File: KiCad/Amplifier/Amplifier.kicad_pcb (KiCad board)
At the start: 2 copper layers, 48 x 53 mm, 30 parts, among them J1 Screw_Terminal_01x03, J2 Screw_Terminal_01x03, Q1 NPN, Q2 NPN, U1 TL074

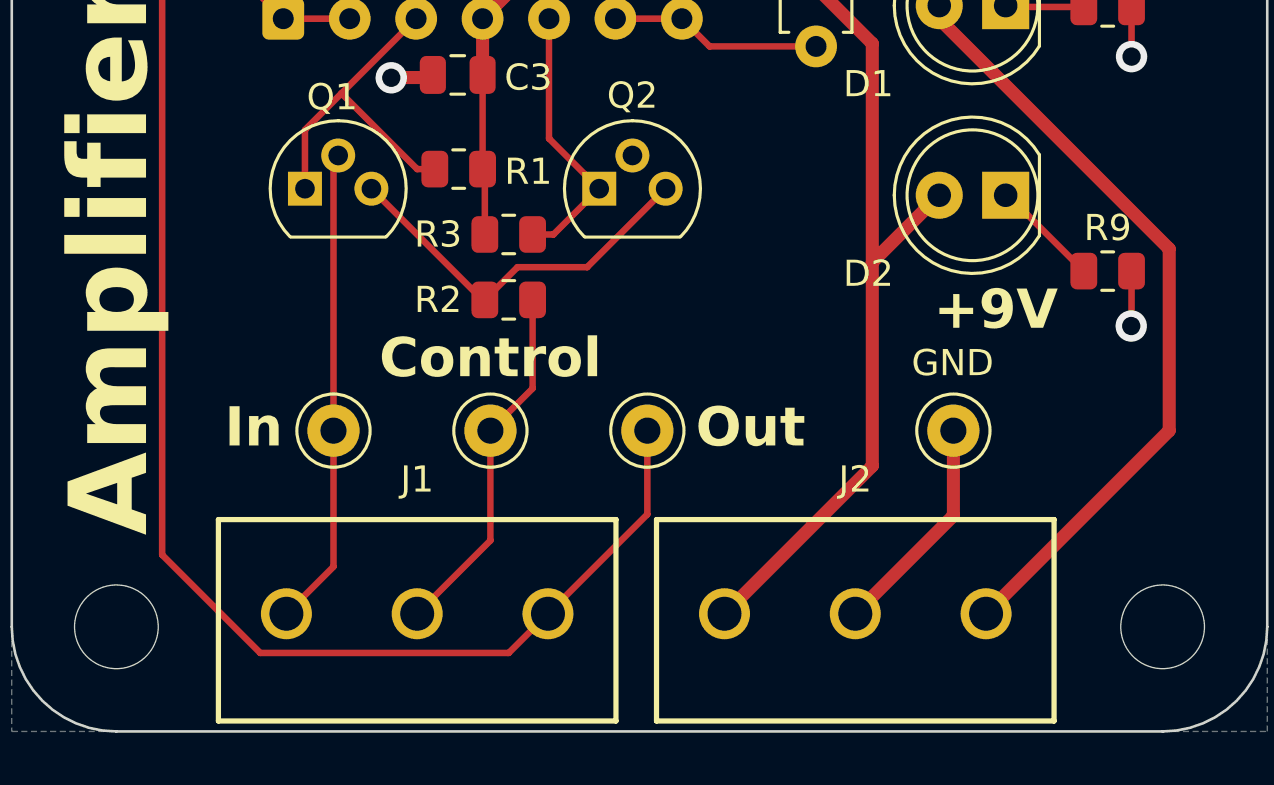
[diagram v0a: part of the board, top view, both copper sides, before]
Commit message: preparation to merge project back into one board
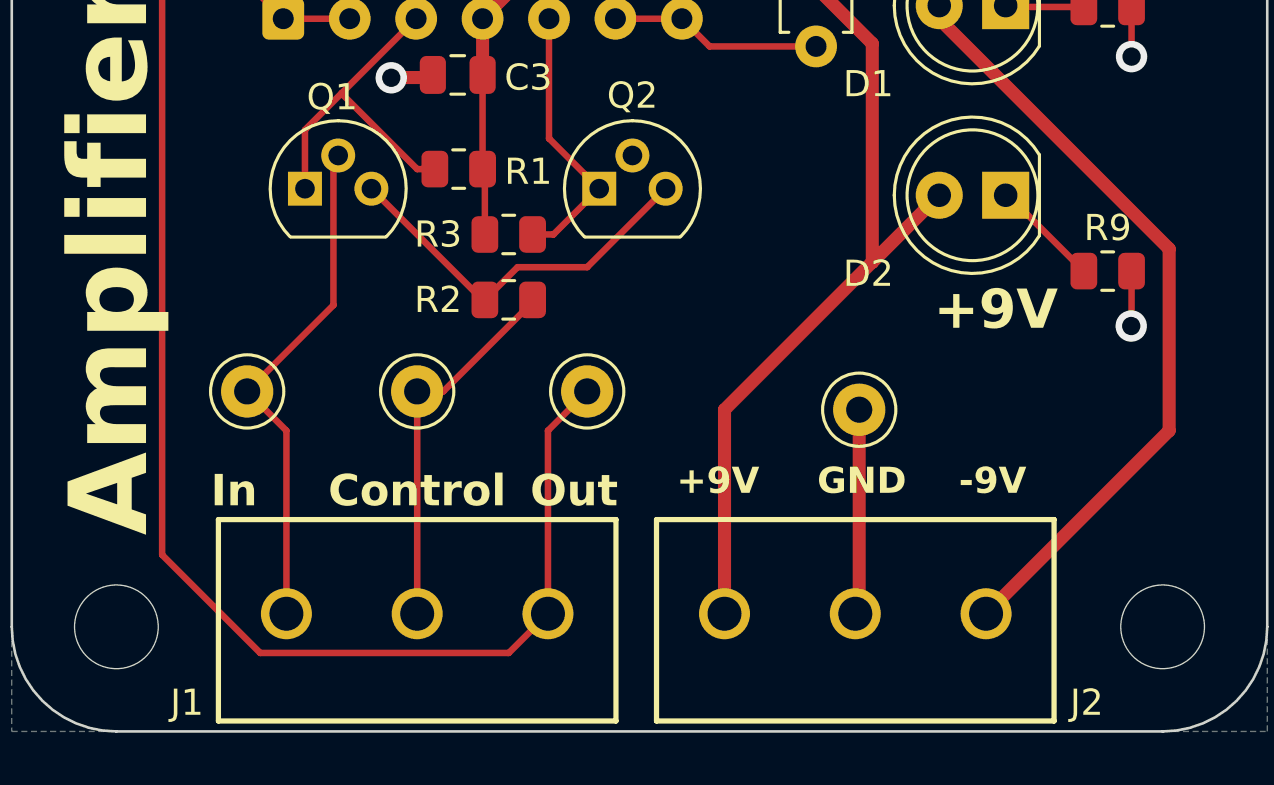
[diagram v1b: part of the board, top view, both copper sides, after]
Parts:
- moved TP4 3.69 mm to (74.4, 75.7)
- moved TP1 3.62 mm to (51.0, 75.0)
- moved TP2 3.18 mm to (57.5, 75.0)
- moved TP3 2.75 mm to (64.0, 75.0)
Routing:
- net /In: track 18.3 -> 19.6 mm
- net GND: track 17.8 -> 17.1 mm
- net /Control: track 13.8 -> 14.4 mm
- net /Out: track 75.2 -> 75.7 mm
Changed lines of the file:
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@@
 			(plot_on_all_layers_selection 0x00000000_00000000_00000000_00000000)
 			(disableapertmacros no)
-			(usegerberextensions no)
+			(usegerberextensions yes)
 			(usegerberattributes yes)
 			(usegerberadvancedattributes yes)
-			(creategerberjobfile yes)
+			(creategerberjobfile no)
 			(dashed_line_dash_ratio 12)
 			(dashed_line_gap_ratio 3)
@@
 			(outputformat 1)
 			(mirror no)
-			(drillshape 1)
+			(drillshape 0)
 			(scaleselection 1)
-			(outputdirectory "")
+			(outputdirectory "../../Build/Aug 20 2026/")
 		)
 	)
@@
 	(footprint "TestPoint:TestPoint_Keystone_5000-5004_Miniature"
 		(layer "F.Cu")
-		(at 78 76.5)
+		(at 74.4 75.7)
 		(descr "Keystone THM Miniature Test Point 5000-5004, http://www.keyelco.com/product-pdf.cfm?p=1309")
 		(tags "Through Hole Mount Test Points")
@@
 	(footprint "TestPoint:TestPoint_Keystone_5000-5004_Miniature"
 		(layer "F.Cu")
-		(at 66.3 76.5)
+		(at 64 75)
 		(descr "Keystone THM Miniature Test Point 5000-5004, http://www.keyelco.com/product-pdf.cfm?p=1309")
 		(tags "Through Hole Mount Test Points")
@@
 	(footprint "TestPoint:TestPoint_Keystone_5000-5004_Miniature"
 		(layer "F.Cu")
-		(at 54.3 76.5)
+		(at 51 75)
 		(descr "Keystone THM Miniature Test Point 5000-5004, http://www.keyelco.com/product-pdf.cfm?p=1309")
 		(tags "Through Hole Mount Test Points")
@@
 		(at 57.5 83.5)
 		(property "Reference" "J1"
-			(at 0 -5.135 0)
+			(at -8.8 3.4 0)
 			(layer "F.SilkS")
 			(effects
@@
 		(at 74.25 83.5)
 		(property "Reference" "J2"
-			(at 0 -5.135 0)
+			(at 8.85 3.4 0)
 			(layer "F.SilkS")
 			(effects
@@
 	(footprint "TestPoint:TestPoint_Keystone_5000-5004_Miniature"
 		(layer "F.Cu")
-		(at 60.3 76.5)
+		(at 57.5 75)
 		(descr "Keystone THM Miniature Test Point 5000-5004, http://www.keyelco.com/product-pdf.cfm?p=1309")
 		(tags "Through Hole Mount Test Points")
@@
 		(layer "Edge.Cuts")
 	)
+	(gr_text "+9V"
+		(at 69 79 0)
+		(layer "F.SilkS")
+		(effects
+			(font
+				(size 1 1)
+				(thickness 0.2)
+				(bold yes)
+			)
+			(justify bottom)
+		)
+	)
 	(gr_text "GND"
-		(at 76.4 74.5 0)
+		(at 74.5 79 0)
 		(layer "F.SilkS")
 		(effects
 			(font
 				(size 1 1)
-				(thickness 0.15)
+				(thickness 0.2)
+				(bold yes)
 			)
-			(justify left bottom)
+			(justify bottom)
+		)
+	)
+	(gr_text "-9V"
+		(at 79.5 79 0)
+		(layer "F.SilkS")
+		(effects
+			(font
+				(size 1 1)
+				(thickness 0.2)
+				(bold yes)
+			)
+			(justify bottom)
 		)
 	)
@@
 		)
 	)
-	(gr_text "+9V"
-		(at 77.25 72.75 0)
+	(gr_text "In"
+		(at 50.5 79.5 0)
 		(layer "F.SilkS")
 		(effects
 			(font
-				(size 1.5 1.5)
-				(thickness 0.3)
+				(size 1.2 1.2)
+				(thickness 0.24)
 				(bold yes)
 			)
-			(justify left bottom)
+			(justify bottom)
 		)
 	)
-	(gr_text "-9V"
-		(at 77.5 57 0)
+	(gr_text "Control"
+		(at 57.5 79.5 0)
 		(layer "F.SilkS")
 		(effects
 			(font
-				(size 1.5 1.5)
-				(thickness 0.3)
+				(size 1.2 1.2)
+				(thickness 0.24)
 				(bold yes)
 			)
-			(justify left bottom)
+			(justify bottom)
 		)
 	)
-	(gr_text "In"
-		(at 51.25 77.25 0)
+	(gr_text "Out"
+		(at 63.5 79.5 0)
 		(layer "F.SilkS")
 		(effects
 			(font
-				(size 1.5 1.5)
-				(thickness 0.3)
+				(size 1.2 1.2)
+				(thickness 0.24)
 				(bold yes)
 			)
@@
 		)
 	)
-	(gr_text "Control"
-		(at 60.3 74.6 0)
+	(gr_text "+9V"
+		(at 77.25 72.75 0)
 		(layer "F.SilkS")
 		(effects
@@
 				(bold yes)
 			)
-			(justify bottom)
+			(justify left bottom)
 		)
 	)
-	(gr_text "Out"
-		(at 70.25 77.25 0)
+	(gr_text "-9V"
+		(at 77.5 57 0)
 		(layer "F.SilkS")
 		(effects
@@
 				(bold yes)
 			)
-			(justify bottom)
+			(justify left bottom)
 		)
 	)
@@
 	)
 	(segment
-		(start 72.2 59)
-		(end 61.75 59)
-		(width 0.5)
-		(layer "F.Cu")
-		(net "+9V")
-	)
-	(segment
 		(start 60 60.75)
 		(end 60 62.9)
@@
 	)
 	(segment
-		(start 74.9 61.7)
-		(end 72.2 59)
+		(start 74.9 70.06)
+		(end 74.9 61.7)
 		(width 0.5)
 		(layer "F.Cu")
@@
 	)
 	(segment
-		(start 69.25 83.5)
-		(end 74.9 77.85)
-		(width 0.5)
+		(start 60.0875 66.5875)
+		(end 60 66.5)
+		(width 0.25)
 		(layer "F.Cu")
 		(net "+9V")
 	)
 	(segment
-		(start 60.0875 66.5875)
-		(end 60 66.5)
-		(width 0.25)
+		(start 69.25 75.7)
+		(end 74.89 70.06)
+		(width 0.5)
 		(layer "F.Cu")
 		(net "+9V")
 	)
 	(segment
-		(start 74.9 70.06)
-		(end 77.46 67.5)
+		(start 61.75 59)
+		(end 60 60.75)
 		(width 0.5)
 		(layer "F.Cu")
@@
 	)
 	(segment
-		(start 61.75 59)
-		(end 60 60.75)
+		(start 74.89 70.06)
+		(end 74.9 70.06)
 		(width 0.5)
 		(layer "F.Cu")
@@
 	)
 	(segment
-		(start 74.9 70.06)
-		(end 74.9 61.7)
+		(start 72.2 59)
+		(end 61.75 59)
 		(width 0.5)
 		(layer "F.Cu")
@@
 	)
 	(segment
-		(start 74.9 77.85)
-		(end 74.9 70.06)
+		(start 74.9 70.06)
+		(end 77.46 67.5)
 		(width 0.5)
 		(layer "F.Cu")
@@
 	)
 	(segment
+		(start 69.25 83.5)
+		(end 69.25 75.7)
+		(width 0.5)
+		(layer "F.Cu")
+		(net "+9V")
+	)
+	(segment
+		(start 74.9 61.7)
+		(end 72.2 59)
+		(width 0.5)
+		(layer "F.Cu")
+		(net "+9V")
+	)
+	(segment
 		(start 62.54 60.75)
 		(end 62.54 65.33)
@@
 	)
 	(segment
-		(start 78 79.75)
-		(end 74.25 83.5)
+		(start 74.4 75.7)
+		(end 74.4 83.35)
 		(width 0.5)
 		(layer "F.Cu")
@@
 	)
 	(segment
-		(start 78 76.5)
-		(end 78 79.75)
+		(start 56.509074 63.009074)
+		(end 56.518148 63)
 		(width 0.5)
 		(layer "F.Cu")
@@
 	)
 	(segment
-		(start 56.509074 63.009074)
-		(end 56.518148 63)
+		(start 74.4 83.35)
+		(end 74.25 83.5)
 		(width 0.5)
 		(layer "F.Cu")
@@
 	)
 	(segment
-		(start 62.5 83.5)
-		(end 66.3 79.7)
-		(width 0.25)
-		(layer "F.Cu")
-		(net "/Out")
-	)
-	(segment
 		(start 55.25 45)
 		(end 51 45)
@@
 	)
 	(segment
-		(start 66.3 79.7)
-		(end 66.3 76.5)
+		(start 62.5 83.5)
+		(end 62.5 76.5)
 		(width 0.25)
 		(layer "F.Cu")
@@
 	)
 	(segment
-		(start 54.3 66.16)
-		(end 54.48 65.98)
+		(start 62.5 76.5)
+		(end 64 75)
 		(width 0.25)
 		(layer "F.Cu")
-		(net "/In")
+		(net "/Out")
 	)
 	(segment
-		(start 54.3 76.5)
-		(end 54.3 66.16)
+		(start 51 75)
+		(end 54.3 71.7)
 		(width 0.25)
 		(layer "F.Cu")
@@
 	(segment
 		(start 52.5 83.5)
-		(end 54.3 81.7)
+		(end 52.5 76.5)
 		(width 0.25)
 		(layer "F.Cu")
@@
 	)
 	(segment
-		(start 54.3 81.7)
-		(end 54.3 76.5)
+		(start 52.5 76.5)
+		(end 51 75)
 		(width 0.25)
 		(layer "F.Cu")
@@
 	)
 	(segment
-		(start 60.3 80.7)
-		(end 60.3 76.5)
+		(start 54.3 66.16)
+		(end 54.48 65.98)
+		(width 0.25)
+		(layer "F.Cu")
+		(net "/In")
+	)
+	(segment
+		(start 54.3 71.7)
+		(end 54.3 66.16)
+		(width 0.25)
+		(layer "F.Cu")
+		(net "/In")
+	)
+	(segment
+		(start 57.5 83.5)
+		(end 57.5 75)
 		(width 0.25)
 		(layer "F.Cu")
@@
 	)
 	(segment
-		(start 61.9125 74.8875)
-		(end 61.9125 71.5)
+		(start 57.5 75)
+		(end 58.5 75)
 		(width 0.25)
 		(layer "F.Cu")
@@
 	)
 	(segment
-		(start 60.3 76.5)
-		(end 61.9125 74.8875)
+		(start 61.9125 71.5875)
+		(end 61.9125 71.5)
 		(width 0.25)
 		(layer "F.Cu")
@@
 	)
 	(segment
-		(start 57.5 83.5)
-		(end 60.3 80.7)
+		(start 58.5 75)
+		(end 61.9125 71.5875)
 		(width 0.25)
 		(layer "F.Cu")

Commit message: merged project into one combined board (excluding the buttons)
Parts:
- removed H1, H2, H3, H4: MountingHole_3.2mm_M3, MountingHole:MountingHole_3.2mm_M3
- added H10: MountingHole, MountingHole:MountingHole_3.2mm_M3, F.Cu at (46.0, 84.0)
- added H11: MountingHole, MountingHole:MountingHole_3.2mm_M3, F.Cu at (86.0, 84.0)
- added H12: MountingHole, MountingHole:MountingHole_3.2mm_M3, F.Cu at (86.0, 39.0)
- added H9: MountingHole, MountingHole:MountingHole_3.2mm_M3, F.Cu at (46.0, 39.0)
- moved G*** 0.54 mm to (45.9, 51.6)
- renumbered C1 to C13, C2 to C14, C3 to C15, D1 to D11, D2 to D12, J1 to J5, J2 to J6, Q1 to Q5, Q2 to Q6, R1 to R23, R2 to R24, R3 to R25, R4 to R26, R5 to R27, R6 to R28, R7 to R29, R8 to R30, R9 to R31, R10 to R32, RV1 to RV9, TP1 to TP13, TP2 to TP14, TP3 to TP15, TP4 to TP16, U1 to U4
